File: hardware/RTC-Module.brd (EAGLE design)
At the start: 19.1 x 19.1 mm, 16 parts, among them Q1 32.768kHz, U1 DS1307

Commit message: Routing and silk changes
1.)  Changed trace routes to go straight away from IC.
2.)  Changed all silk to vector
3.)  Made pin labels smaller to avoid interfering with resistors.
3.) Standardized trace width to .01
4.) Moved R1 to the left and rerouted SQW trace.
5.) Added tRestrict under IC.
6.) Moved name silk over to make room for vcc via.
7.) Moved OSHW logo to top corner and moved sparkfun name on to board.
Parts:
- moved LOGO1 18.1 mm to (16.3, 16.3)
- moved LOGO2 15.0 mm to (11.9, 3.43), flipped to the bottom
- moved R1 1.30 mm to (7.62, 7.37)
- moved R2 0.25 mm to (3.81, 7.37)
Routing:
- net N$1: track 2.16 -> 5.16 mm
- net N$4: track 7.46 -> 9.04 mm, vias 0 -> 1
- net SQW: track 9.42 -> 10.6 mm
- net N$3: track 16.8 -> 15.8 mm, vias 2 -> 3
- net N$2: track 8.96 -> 9.92 mm
- net SCL: track 10.3 -> 9.42 mm

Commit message: Removed Sparkfun web logo
Just not enough room for it. The SF flame should suffice.
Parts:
- removed LOGO2: SFE_LOGO_NAME_FLAME.1_INCH, SparkFun-Aesthetics:SFE_LOGO_NAME_FLAME_.1
- moved LOGO1 18.1 mm to (2.29, 4.83)
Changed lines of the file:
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@@
 <?xml version="1.0" encoding="utf-8"?>
 <!DOCTYPE eagle SYSTEM "eagle.dtd">
-<eagle version="6.4">
+<eagle version="6.5.0">
 <drawing>
 <settings>
@@
 <element name="SJ1" library="SparkFun-Passives" package="SJ_2S" value="" x="16.51" y="6.35"/>
 <element name="FRAME2" library="SparkFun-Aesthetics" package="CREATIVE_COMMONS" value="FRAME-LETTER" x="21.59" y="-15.24"/>
-<element name="LOGO1" library="SparkFun-Aesthetics" package="OSHW-LOGO-S" value="OSHW-LOGOS" x="16.256" y="16.256" rot="MR0"/>
-<element name="LOGO2" library="SparkFun-Aesthetics" package="SFE_LOGO_NAME_FLAME_.1" value="SFE_LOGO_NAME_FLAME.1_INCH" x="11.938" y="3.429" rot="MR0"/>
+<element name="LOGO1" library="SparkFun-Aesthetics" package="OSHW-LOGO-S" value="OSHW-LOGOS" x="2.286" y="4.826" rot="MR0"/>
 </elements>
 <signals>

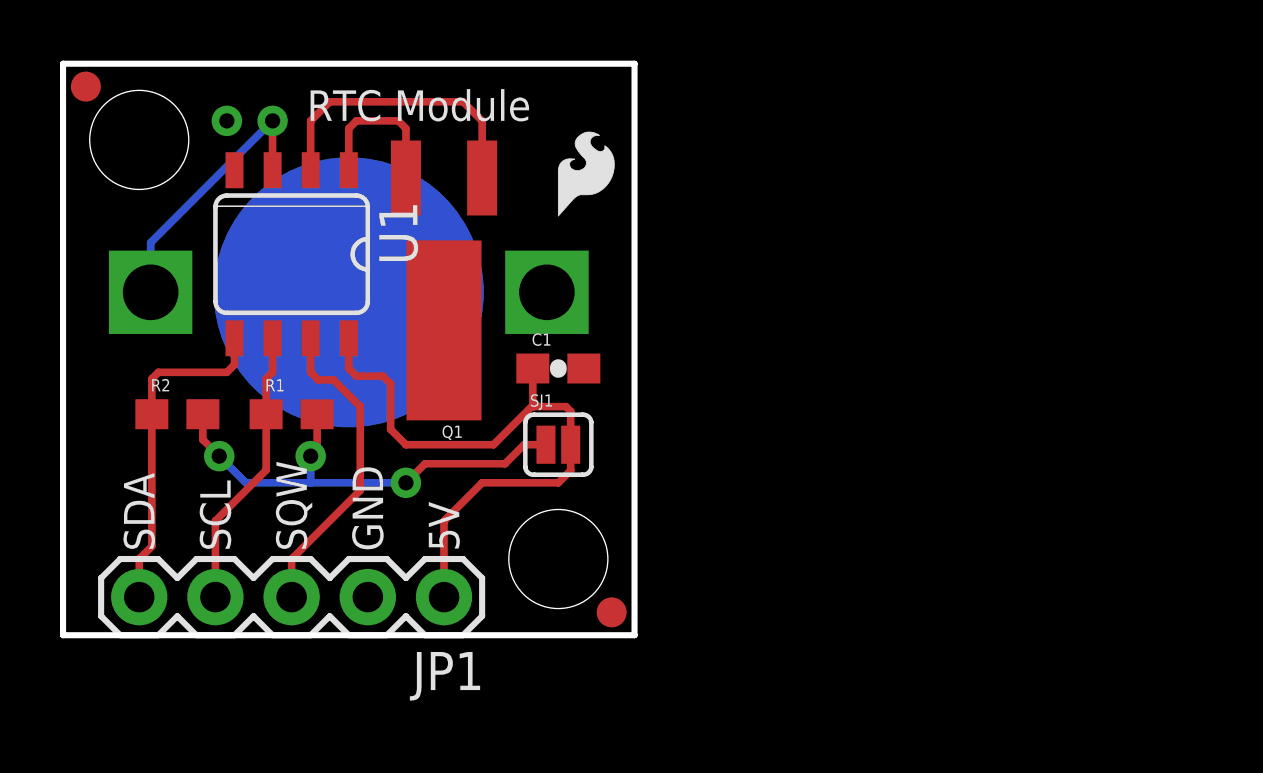
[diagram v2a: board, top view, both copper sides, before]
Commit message: Fixed I2C jumper. Silk mods. Removed restrict polygon.
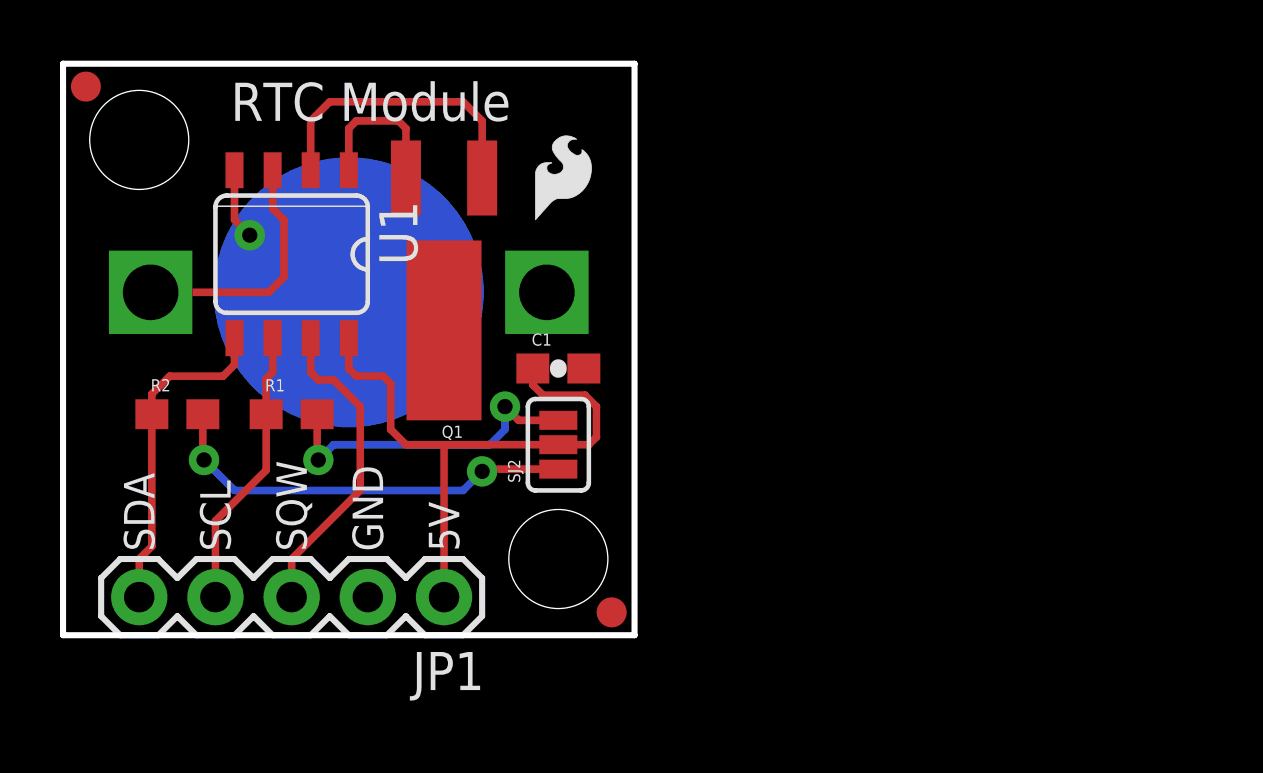
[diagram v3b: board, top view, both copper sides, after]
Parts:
- removed SJ1: (no value), SparkFun-Passives:SJ_2S
- added SJ2: (no value), SparkFun-Passives:SJ_3_PASTE1&2&3
- moved U$1 0.77 mm to (15.7, 13.8)
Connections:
- removed net N$3: R1.2, R2.2, SJ1.1
- new net N$5: R1.2, SJ2.3
- new net N$6: R2.2, SJ2.1
- net 5V: now also SJ2.2; no longer SJ1.2
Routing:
- net N$3: track 15.8 -> 0.00 mm, vias 3 -> 0
- net N$6: track 0.00 -> 14.1 mm, vias 0 -> 2
- net N$5: track 0.00 -> 10.9 mm, vias 0 -> 2
- net GND: track 0.00 -> 6.47 mm
- net 5V: track 21.6 -> 20.4 mm
- net N$4: track 9.04 -> 8.38 mm, vias 1 -> 0
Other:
- board text added: "DS1307"
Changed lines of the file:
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@@
 <layer number="47" name="Measures" color="7" fill="1" visible="no" active="yes"/>
 <layer number="48" name="Document" color="7" fill="1" visible="no" active="yes"/>
-<layer number="49" name="Reference" color="7" fill="1" visible="yes" active="yes"/>
+<layer number="49" name="Reference" color="7" fill="1" visible="no" active="yes"/>
 <layer number="50" name="dxf" color="7" fill="1" visible="no" active="yes"/>
 <layer number="51" name="tDocu" color="6" fill="1" visible="yes" active="yes"/>
@@
 <text x="5.588" y="2.794" size="1.016" layer="21" font="vector" ratio="15" rot="R90">SCL</text>
 <text x="3.048" y="2.794" size="1.016" layer="21" font="vector" ratio="15" rot="R90">SDA</text>
-<text x="8.128" y="17.145" size="1.016" layer="21" font="vector" ratio="15">RTC Module</text>
+<text x="5.588" y="17.145" size="1.27" layer="21" font="vector" ratio="15">RTC Module</text>
 <text x="16.764" y="7.112" size="0.2032" layer="27">.1 uF</text>
 <text x="53.34" y="-15.24" size="1.778" layer="51" font="vector" ratio="15">N. Seidle</text>
-<rectangle x1="5.334" y1="11.049" x2="9.906" y2="14.351" layer="41"/>
+<text x="12.954" y="3.175" size="1.27" layer="22" font="vector" ratio="15" rot="MR0">DS1307</text>
 </plain>
 <attributes>
@@
 </autorouter>
 <elements>
-<element name="U$1" library="SparkFun" package="SFE-LOGO-FLAME" value="LOGO-SFESK" x="16.51" y="13.97"/>
+<element name="U$1" library="SparkFun" package="SFE-LOGO-FLAME" value="LOGO-SFESK" x="15.748" y="13.843"/>
 <element name="U$6" library="SparkFun" package="STAND-OFF" value="STAND-OFF" x="16.51" y="2.54"/>
 <element name="U$7" library="SparkFun" package="STAND-OFF" value="STAND-OFF" x="2.54" y="16.51"/>
@@
 <attribute name="PROD_ID" value="RES-07857" x="3.81" y="7.366" size="1.778" layer="27" font="vector" ratio="15" display="off"/>
 </element>
-<element name="SJ1" library="SparkFun-Passives" package="SJ_2S" value="" x="16.51" y="6.35"/>
 <element name="FRAME2" library="SparkFun-Aesthetics" package="CREATIVE_COMMONS" value="FRAME-LETTER" x="21.59" y="-15.24"/>
 <element name="LOGO1" library="SparkFun-Aesthetics" package="OSHW-LOGO-S" value="OSHW-LOGOS" x="2.286" y="4.826" rot="MR0"/>
+<element name="SJ2" library="SparkFun-Passives" package="SJ_3_PASTE1&amp;2&amp;3" value="" x="16.51" y="6.35" rot="R90"/>
 </elements>
 <signals>
@@
 <vertex x="19.05" y="19.05"/>
 </polygon>
-<via x="5.461" y="17.145" extent="1-16" drill="0.508"/>
+<via x="6.223" y="13.335" extent="1-16" drill="0.508"/>
+<wire x1="9.525" y1="11.43" x2="8.128" y2="11.43" width="0.254" layer="16"/>
+<wire x1="8.128" y1="11.43" x2="6.223" y2="13.335" width="0.254" layer="16"/>
+<wire x1="5.715" y1="15.5" x2="5.715" y2="13.843" width="0.254" layer="1"/>
+<wire x1="5.715" y1="13.843" x2="6.223" y2="13.335" width="0.254" layer="1"/>
 </signal>
 <signal name="N$1">
@@
 <contactref element="U1" pad="3"/>
 <contactref element="BAT1" pad="VCC@1"/>
-<wire x1="6.985" y1="15.5" x2="6.985" y2="17.145" width="0.254" layer="1"/>
-<wire x1="2.921" y1="11.43" x2="2.921" y2="13.081" width="0.254" layer="16"/>
-<wire x1="2.921" y1="13.081" x2="6.985" y2="17.145" width="0.254" layer="16"/>
-<via x="6.985" y="17.145" extent="1-16" drill="0.508"/>
+<wire x1="6.985" y1="15.5" x2="6.985" y2="14.224" width="0.254" layer="1"/>
+<wire x1="6.985" y1="14.224" x2="7.366" y2="13.843" width="0.254" layer="1"/>
+<wire x1="7.366" y1="13.843" x2="7.366" y2="11.938" width="0.254" layer="1"/>
+<wire x1="7.366" y1="11.938" x2="6.858" y2="11.43" width="0.254" layer="1"/>
+<wire x1="6.858" y1="11.43" x2="2.921" y2="11.43" width="0.254" layer="1"/>
 </signal>
 <signal name="SQW">
@@
 <contactref element="U1" pad="5"/>
 <contactref element="R2" pad="1"/>
-<wire x1="5.715" y1="9.9" x2="5.715" y2="9.017" width="0.254" layer="1"/>
-<wire x1="5.715" y1="9.017" x2="5.461" y2="8.763" width="0.254" layer="1"/>
-<wire x1="5.461" y1="8.763" x2="3.175" y2="8.763" width="0.254" layer="1"/>
-<wire x1="3.175" y1="8.763" x2="2.96" y2="8.548" width="0.254" layer="1"/>
-<wire x1="2.96" y1="7.366" x2="2.96" y2="8.548" width="0.254" layer="1"/>
 <wire x1="2.96" y1="7.366" x2="2.96" y2="2.96" width="0.254" layer="1"/>
 <wire x1="2.96" y1="2.96" x2="2.54" y2="2.54" width="0.254" layer="1"/>
 <wire x1="2.54" y1="2.54" x2="2.54" y2="1.27" width="0.254" layer="1"/>
-</signal>
-<signal name="N$3">
-<contactref element="SJ1" pad="1"/>
-<contactref element="R2" pad="2"/>
-<contactref element="R1" pad="2"/>
-<via x="11.43" y="5.08" extent="1-16" drill="0.508"/>
-<via x="5.207" y="5.969" extent="1-16" drill="0.508"/>
-<wire x1="4.66" y1="7.366" x2="4.66" y2="6.516" width="0.254" layer="1"/>
-<wire x1="11.43" y1="5.08" x2="8.255" y2="5.08" width="0.254" layer="16"/>
-<wire x1="8.255" y1="5.08" x2="6.096" y2="5.08" width="0.254" layer="16"/>
-<wire x1="16.0981" y1="6.35" x2="15.367" y2="6.35" width="0.254" layer="1"/>
-<wire x1="15.367" y1="6.35" x2="14.732" y2="5.715" width="0.254" layer="1"/>
-<wire x1="14.732" y1="5.715" x2="12.065" y2="5.715" width="0.254" layer="1"/>
-<wire x1="12.065" y1="5.715" x2="11.43" y2="5.08" width="0.254" layer="1"/>
-<wire x1="4.66" y1="6.516" x2="5.207" y2="5.969" width="0.254" layer="1"/>
-<wire x1="6.096" y1="5.08" x2="5.207" y2="5.969" width="0.254" layer="16"/>
-<via x="8.255" y="5.969" extent="1-16" drill="0.508"/>
-<wire x1="8.255" y1="5.969" x2="8.255" y2="5.08" width="0.254" layer="16"/>
-<wire x1="8.47" y1="7.366" x2="8.47" y2="6.184" width="0.254" layer="1"/>
-<wire x1="8.47" y1="6.184" x2="8.255" y2="5.969" width="0.254" layer="1"/>
+<wire x1="5.715" y1="9.9" x2="5.715" y2="9.017" width="0.254" layer="1"/>
+<wire x1="5.715" y1="9.017" x2="5.334" y2="8.636" width="0.254" layer="1"/>
+<wire x1="5.334" y1="8.636" x2="3.556" y2="8.636" width="0.254" layer="1"/>
+<wire x1="3.556" y1="8.636" x2="2.96" y2="8.04" width="0.254" layer="1"/>
+<wire x1="2.96" y1="7.366" x2="2.96" y2="8.04" width="0.254" layer="1"/>
 </signal>
 <signal name="5V">
 <contactref element="JP1" pad="1"/>
-<contactref element="SJ1" pad="2"/>
 <contactref element="U1" pad="8"/>
 <contactref element="C1" pad="1"/>
-<wire x1="16.9219" y1="5.4919" x2="16.51" y2="5.08" width="0.254" layer="1"/>
-<wire x1="16.51" y1="5.08" x2="13.97" y2="5.08" width="0.254" layer="1"/>
-<wire x1="13.97" y1="5.08" x2="12.7" y2="3.81" width="0.254" layer="1"/>
-<wire x1="12.7" y1="3.81" x2="12.7" y2="1.27" width="0.254" layer="1"/>
-<wire x1="15.66" y1="7.659" x2="14.351" y2="6.35" width="0.254" layer="1"/>
-<wire x1="14.351" y1="6.35" x2="11.43" y2="6.35" width="0.254" layer="1"/>
-<wire x1="11.43" y1="6.35" x2="10.922" y2="6.858" width="0.254" layer="1"/>
-<wire x1="16.9219" y1="6.35" x2="16.9219" y2="7.4621" width="0.254" layer="1"/>
-<wire x1="16.9219" y1="7.4621" x2="16.764" y2="7.62" width="0.254" layer="1"/>
-<wire x1="16.764" y1="7.62" x2="15.699" y2="7.62" width="0.254" layer="1"/>
-<wire x1="15.699" y1="7.62" x2="15.66" y2="7.659" width="0.254" layer="1"/>
-<wire x1="15.66" y1="8.89" x2="15.66" y2="7.659" width="0.254" layer="1"/>
-<wire x1="16.9219" y1="6.35" x2="16.9219" y2="5.4919" width="0.254" layer="1"/>
 <wire x1="9.525" y1="9.9" x2="9.525" y2="8.89" width="0.254" layer="1"/>
 <wire x1="9.525" y1="8.89" x2="9.779" y2="8.636" width="0.254" layer="1"/>
@@
 <wire x1="10.668" y1="8.636" x2="10.922" y2="8.382" width="0.254" layer="1"/>
 <wire x1="10.922" y1="8.382" x2="10.922" y2="6.858" width="0.254" layer="1"/>
+<contactref element="SJ2" pad="2"/>
+<wire x1="16.51" y1="6.35" x2="12.7" y2="6.35" width="0.254" layer="1"/>
+<wire x1="12.7" y1="6.35" x2="11.43" y2="6.35" width="0.254" layer="1"/>
+<wire x1="11.43" y1="6.35" x2="10.922" y2="6.858" width="0.254" layer="1"/>
+<wire x1="12.7" y1="1.27" x2="12.7" y2="6.35" width="0.254" layer="1"/>
+<wire x1="15.66" y1="8.89" x2="15.66" y2="8.343" width="0.254" layer="1"/>
+<wire x1="15.66" y1="8.343" x2="16.002" y2="8.001" width="0.254" layer="1"/>
+<wire x1="16.002" y1="8.001" x2="17.399" y2="8.001" width="0.254" layer="1"/>
+<wire x1="17.399" y1="8.001" x2="17.78" y2="7.62" width="0.254" layer="1"/>
+<wire x1="17.78" y1="7.62" x2="17.78" y2="6.604" width="0.254" layer="1"/>
+<wire x1="17.78" y1="6.604" x2="17.526" y2="6.35" width="0.254" layer="1"/>
+<wire x1="17.526" y1="6.35" x2="16.51" y2="6.35" width="0.254" layer="1"/>
+</signal>
+<signal name="N$5">
+<contactref element="R1" pad="2"/>
+<contactref element="SJ2" pad="3"/>
+<wire x1="16.51" y1="7.1628" x2="15.1892" y2="7.1628" width="0.254" layer="1"/>
+<wire x1="15.1892" y1="7.1628" x2="14.732" y2="7.62" width="0.254" layer="1"/>
+<via x="14.732" y="7.62" extent="1-16" drill="0.508"/>
+<wire x1="14.732" y1="7.62" x2="14.732" y2="6.858" width="0.254" layer="16"/>
+<wire x1="14.732" y1="6.858" x2="14.224" y2="6.35" width="0.254" layer="16"/>
+<wire x1="14.224" y1="6.35" x2="9.017" y2="6.35" width="0.254" layer="16"/>
+<wire x1="9.017" y1="6.35" x2="8.509" y2="5.842" width="0.254" layer="16"/>
+<via x="8.509" y="5.842" extent="1-16" drill="0.508"/>
+<wire x1="8.47" y1="7.366" x2="8.47" y2="5.881" width="0.254" layer="1"/>
+<wire x1="8.47" y1="5.881" x2="8.509" y2="5.842" width="0.254" layer="1"/>
+</signal>
+<signal name="N$6">
+<contactref element="R2" pad="2"/>
+<contactref element="SJ2" pad="1"/>
+<wire x1="16.51" y1="5.5372" x2="14.0462" y2="5.5372" width="0.254" layer="1"/>
+<wire x1="13.335" y1="4.826" x2="5.715" y2="4.826" width="0.254" layer="16"/>
+<wire x1="5.715" y1="4.826" x2="4.699" y2="5.842" width="0.254" layer="16"/>
+<wire x1="4.66" y1="7.366" x2="4.66" y2="5.881" width="0.254" layer="1"/>
+<wire x1="4.66" y1="5.881" x2="4.699" y2="5.842" width="0.254" layer="1"/>
+<via x="4.699" y="5.842" extent="1-16" drill="0.508"/>
+<wire x1="14.0462" y1="5.5372" x2="13.97" y2="5.461" width="0.254" layer="1"/>
+<via x="13.97" y="5.461" extent="1-16" drill="0.508"/>
+<wire x1="13.97" y1="5.461" x2="13.335" y2="4.826" width="0.254" layer="16"/>
 </signal>
 </signals>
+<errors>
+</errors>
 </board>
 </drawing>

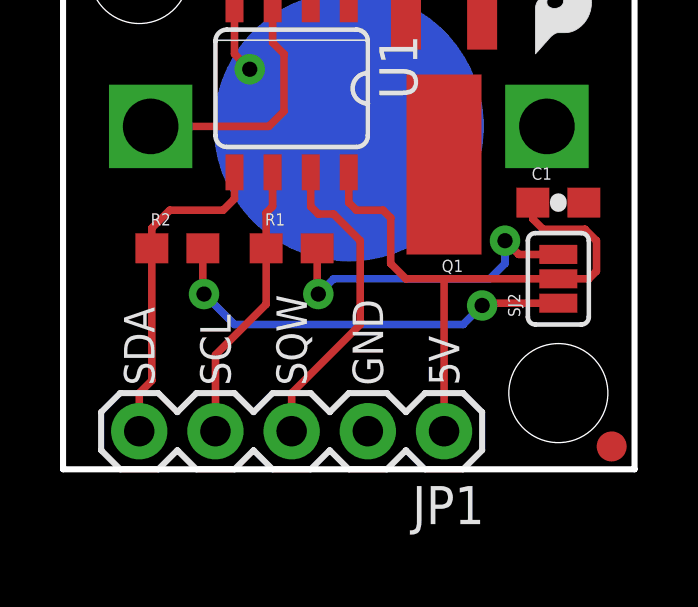
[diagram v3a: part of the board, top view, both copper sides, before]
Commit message: Small changes to silk. Add prototype files.
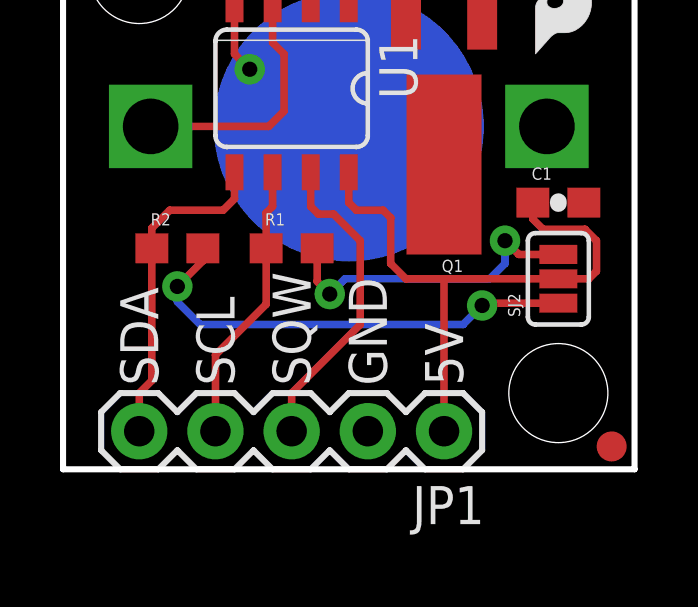
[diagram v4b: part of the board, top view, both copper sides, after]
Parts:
- moved LOGO1 0.68 mm to (2.54, 4.19)
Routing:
- net N$6: track 14.1 -> 15.4 mm
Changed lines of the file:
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@@
 <wire x1="-0.254" y1="9.525" x2="19.812" y2="9.525" width="0.254" layer="51"/>
 <wire x1="9.525" y1="19.431" x2="9.525" y2="-0.762" width="0.254" layer="51"/>
-<text x="13.208" y="2.794" size="1.016" layer="21" font="vector" ratio="15" rot="R90">5V</text>
-<text x="10.668" y="2.794" size="1.016" layer="21" font="vector" ratio="15" rot="R90">GND</text>
-<text x="8.128" y="2.794" size="1.016" layer="21" font="vector" ratio="15" rot="R90">SQW</text>
-<text x="5.588" y="2.794" size="1.016" layer="21" font="vector" ratio="15" rot="R90">SCL</text>
-<text x="3.048" y="2.794" size="1.016" layer="21" font="vector" ratio="15" rot="R90">SDA</text>
+<text x="13.335" y="2.794" size="1.27" layer="21" font="vector" ratio="15" rot="R90">5V</text>
+<text x="10.795" y="2.794" size="1.27" layer="21" font="vector" ratio="15" rot="R90">GND</text>
+<text x="8.255" y="2.794" size="1.27" layer="21" font="vector" ratio="15" rot="R90">SQW</text>
+<text x="5.715" y="2.794" size="1.27" layer="21" font="vector" ratio="15" rot="R90">SCL</text>
+<text x="3.175" y="2.794" size="1.27" layer="21" font="vector" ratio="15" rot="R90">SDA</text>
 <text x="5.588" y="17.145" size="1.27" layer="21" font="vector" ratio="15">RTC Module</text>
 <text x="16.764" y="7.112" size="0.2032" layer="27">.1 uF</text>
@@
 </class>
 </classes>
-<designrules name="SparkFun">
+<designrules name="SparkFun *">
 <description language="en">&lt;b&gt;EAGLE Design Rules&lt;/b&gt;
 &lt;p&gt;
@@
 <param name="dpGapFactor" value="2.5"/>
 <param name="checkGrid" value="0"/>
-<param name="checkAngle" value="0"/>
+<param name="checkAngle" value="1"/>
 <param name="checkFont" value="1"/>
 <param name="checkRestrict" value="1"/>
@@
 </element>
 <element name="FRAME2" library="SparkFun-Aesthetics" package="CREATIVE_COMMONS" value="FRAME-LETTER" x="21.59" y="-15.24"/>
-<element name="LOGO1" library="SparkFun-Aesthetics" package="OSHW-LOGO-S" value="OSHW-LOGOS" x="2.286" y="4.826" rot="MR0"/>
+<element name="LOGO1" library="SparkFun-Aesthetics" package="OSHW-LOGO-S" value="OSHW-LOGOS" x="2.54" y="4.191" rot="MR0"/>
 <element name="SJ2" library="SparkFun-Passives" package="SJ_3_PASTE1&amp;2&amp;3" value="" x="16.51" y="6.35" rot="R90"/>
 </elements>
@@
 <wire x1="14.732" y1="7.62" x2="14.732" y2="6.858" width="0.254" layer="16"/>
 <wire x1="14.732" y1="6.858" x2="14.224" y2="6.35" width="0.254" layer="16"/>
-<wire x1="14.224" y1="6.35" x2="9.017" y2="6.35" width="0.254" layer="16"/>
-<wire x1="9.017" y1="6.35" x2="8.509" y2="5.842" width="0.254" layer="16"/>
-<via x="8.509" y="5.842" extent="1-16" drill="0.508"/>
-<wire x1="8.47" y1="7.366" x2="8.47" y2="5.881" width="0.254" layer="1"/>
-<wire x1="8.47" y1="5.881" x2="8.509" y2="5.842" width="0.254" layer="1"/>
+<wire x1="14.224" y1="6.35" x2="9.398" y2="6.35" width="0.254" layer="16"/>
+<via x="8.89" y="5.842" extent="1-16" drill="0.508"/>
+<wire x1="8.47" y1="7.366" x2="8.47" y2="6.262" width="0.254" layer="1"/>
+<wire x1="8.47" y1="6.262" x2="8.89" y2="5.842" width="0.254" layer="1"/>
+<wire x1="9.398" y1="6.35" x2="8.89" y2="5.842" width="0.254" layer="16"/>
 </signal>
 <signal name="N$6">
@@
 <contactref element="SJ2" pad="1"/>
 <wire x1="16.51" y1="5.5372" x2="14.0462" y2="5.5372" width="0.254" layer="1"/>
-<wire x1="13.335" y1="4.826" x2="5.715" y2="4.826" width="0.254" layer="16"/>
-<wire x1="5.715" y1="4.826" x2="4.699" y2="5.842" width="0.254" layer="16"/>
-<wire x1="4.66" y1="7.366" x2="4.66" y2="5.881" width="0.254" layer="1"/>
-<wire x1="4.66" y1="5.881" x2="4.699" y2="5.842" width="0.254" layer="1"/>
-<via x="4.699" y="5.842" extent="1-16" drill="0.508"/>
+<wire x1="13.335" y1="4.826" x2="4.572" y2="4.826" width="0.254" layer="16"/>
 <wire x1="14.0462" y1="5.5372" x2="13.97" y2="5.461" width="0.254" layer="1"/>
 <via x="13.97" y="5.461" extent="1-16" drill="0.508"/>
 <wire x1="13.97" y1="5.461" x2="13.335" y2="4.826" width="0.254" layer="16"/>
+<via x="3.81" y="6.096" extent="1-16" drill="0.508"/>
+<wire x1="3.81" y1="6.096" x2="3.81" y2="5.588" width="0.254" layer="16"/>
+<wire x1="3.81" y1="5.588" x2="4.572" y2="4.826" width="0.254" layer="16"/>
+<wire x1="4.66" y1="7.366" x2="4.66" y2="6.946" width="0.254" layer="1"/>
+<wire x1="4.66" y1="6.946" x2="3.81" y2="6.096" width="0.254" layer="1"/>
 </signal>
 </signals>
